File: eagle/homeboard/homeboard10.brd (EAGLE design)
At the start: 100 x 80 mm, 99 parts, among them IC1 XCF02S, IC2 25LC080SN, IC3 ATMEGA32U2-TQFP, Q5 BC848SMD, Q6 BC848SMD, Q7 BC848SMD, Q8 BC848SMD, T1 BSS138, T2 BC848, T3 BSS138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

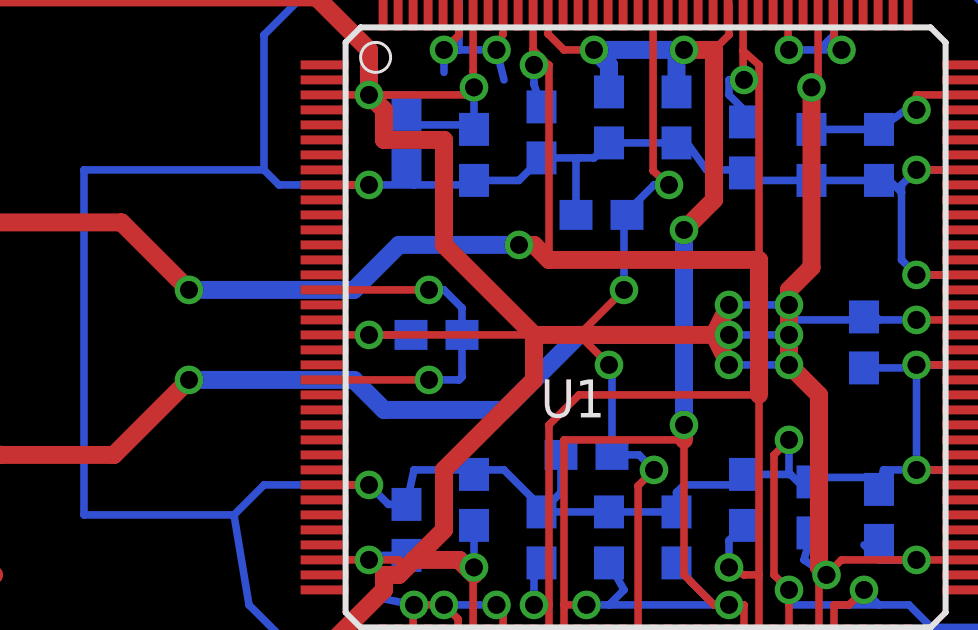
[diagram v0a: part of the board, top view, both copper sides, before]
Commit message: fpga all capactored up
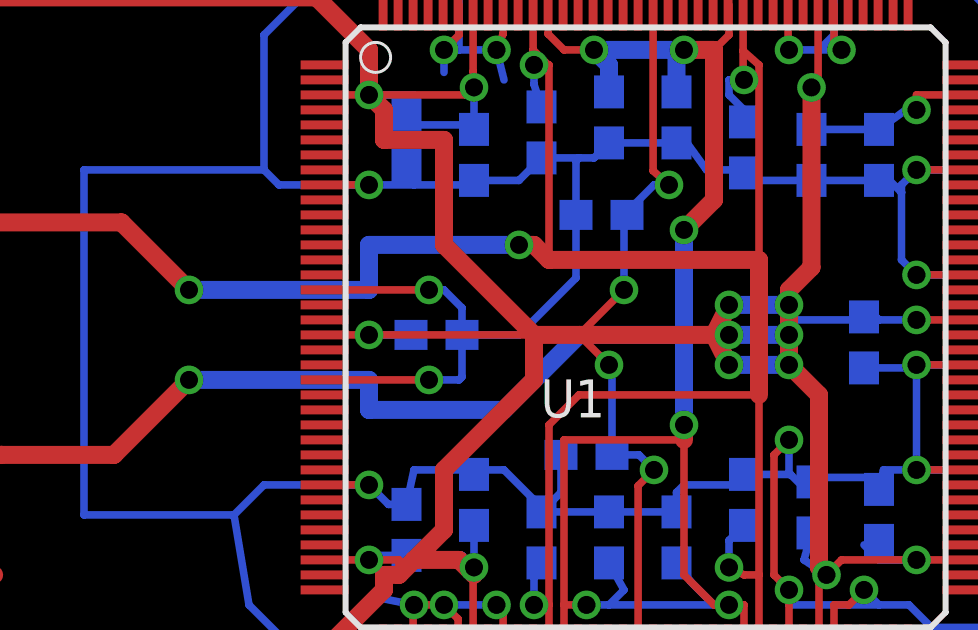
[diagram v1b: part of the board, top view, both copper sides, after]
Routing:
- net GND: track 510.0 -> 516.7 mm
- net VCC: track 334.7 -> 336.7 mm
- net VCCAUX: track 90.3 -> 91.2 mm
- net VCCINT: track 87.4 -> 88.0 mm
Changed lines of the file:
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@@
 <wire x1="29.5" y1="39.5" x2="28.5" y2="39.5" width="0.254" layer="16"/>
 <wire x1="29.6" y1="41" x2="29.6" y2="41.9" width="0.254" layer="16"/>
+<wire x1="33.4" y1="45" x2="33.4" y2="42.9" width="0.254" layer="16"/>
+<wire x1="33.4" y1="42.9" x2="31.5" y2="41" width="0.254" layer="16"/>
+<wire x1="31.5" y1="41" x2="29.6" y2="41" width="0.254" layer="16"/>
 <wire x1="96.05" y1="71" x2="95.55" y2="76" width="0" layer="19" extent="1-1"/>
 <wire x1="96.55" y1="67.5" x2="96.05" y2="71" width="0" layer="19" extent="1-1"/>
@@
 <wire x1="29.47" y1="51.95" x2="29.5" y2="52" width="0" layer="19" extent="1-1"/>
 <wire x1="44.335" y1="7.75" x2="44.5" y2="7.75" width="0" layer="19" extent="1-1"/>
-<wire x1="28.5" y1="39.5" x2="28" y2="36.5" width="0" layer="19" extent="16-16"/>
 <wire x1="98.3" y1="2.25" x2="81.27" y2="16.1284" width="0" layer="19" extent="1-1"/>
 </signal>
@@
 <wire x1="43" y1="41.6" x2="43.4" y2="41.6" width="0.254" layer="16"/>
 <wire x1="43.4" y1="41.6" x2="43.5" y2="41.5" width="0.254" layer="16"/>
-<wire x1="38.5" y1="42" x2="40.5" y2="42" width="0.254" layer="16"/>
-<wire x1="41.5" y1="40" x2="41.5" y2="39" width="0" layer="19" extent="1-16"/>
-<wire x1="41.5" y1="39" x2="40.5" y2="39" width="0" layer="19" extent="1-16"/>
-<wire x1="40.5" y1="42" x2="41.5" y2="40" width="0" layer="19" extent="1-16"/>
-<wire x1="40.5" y1="40" x2="38.5" y2="40" width="0.254" layer="16"/>
-<wire x1="38.5" y1="41" x2="40.5" y2="41" width="0.254" layer="16"/>
+<wire x1="38.5" y1="41" x2="40.5" y2="41" width="0.6" layer="16"/>
 <via x="38.5" y="42" extent="1-16" drill="0.6" shape="square"/>
 <wire x1="38.5" y1="42" x2="38" y2="41" width="0.6" layer="1"/>
@@
 <wire x1="41.5" y1="39" x2="41.5" y2="33.25" width="0.6" layer="1"/>
 <wire x1="41.5" y1="33.25" x2="41.75" y2="33" width="0.6" layer="1"/>
+<wire x1="40.5" y1="40" x2="40.5" y2="41" width="0.6" layer="1"/>
+<via x="40.5" y="41" extent="1-16" drill="0.6" shape="square"/>
+<wire x1="40.5" y1="41" x2="40.5" y2="42" width="0.6" layer="1"/>
+<wire x1="38.5" y1="40" x2="40.5" y2="40" width="0.6" layer="16"/>
+<wire x1="38.5" y1="42" x2="40.5" y2="42" width="0.6" layer="16"/>
+<wire x1="40.5" y1="42" x2="40.5" y2="40" width="0.6" layer="16"/>
 <wire x1="90.9" y1="64.5" x2="92.45" y2="68" width="0" layer="19" extent="1-16"/>
 <wire x1="73.984" y1="67.5094" x2="90.9" y2="64.5" width="0" layer="19" extent="1-16"/>
@@
 <wire x1="35.1" y1="45" x2="35" y2="45" width="0" layer="19" extent="16-16"/>
 <wire x1="18.5" y1="22" x2="18.75" y2="21.85" width="0" layer="19" extent="16-16"/>
-<wire x1="40.5" y1="40" x2="40.5" y2="41" width="0.6" layer="1"/>
-<via x="40.5" y="41" extent="1-16" drill="0.6" shape="square"/>
-<wire x1="40.5" y1="41" x2="40.5" y2="42" width="0.6" layer="1"/>
 </signal>
 <signal name="TCK">
@@
 <wire x1="18" y1="37" x2="20.5" y2="39.5" width="0.6" layer="1"/>
 <via x="20.5" y="39.5" extent="1-16" drill="0.6" shape="square"/>
-<wire x1="20.5" y1="39.5" x2="26" y2="39.5" width="0.6" layer="16"/>
-<wire x1="26" y1="39.5" x2="27" y2="38.5" width="0.6" layer="16"/>
-<wire x1="27" y1="38.5" x2="31" y2="38.5" width="0.6" layer="16"/>
+<wire x1="20.5" y1="39.5" x2="26.5" y2="39.5" width="0.6" layer="16"/>
+<wire x1="26.5" y1="39.5" x2="26.5" y2="38.5" width="0.6" layer="16"/>
+<wire x1="26.5" y1="38.5" x2="31" y2="38.5" width="0.6" layer="16"/>
 <wire x1="31" y1="38.5" x2="33.5" y2="41" width="0.6" layer="16"/>
 <wire x1="33.5" y1="41" x2="37" y2="41" width="0.6" layer="16"/>
@@
 <wire x1="18.25" y1="44.75" x2="20.5" y2="42.5" width="0.6" layer="1"/>
 <via x="20.5" y="42.5" extent="1-16" drill="0.6" shape="square"/>
-<wire x1="20.5" y1="42.5" x2="26" y2="42.5" width="0.6" layer="16"/>
-<wire x1="26" y1="42.5" x2="27.5" y2="44" width="0.6" layer="16"/>
-<wire x1="27.5" y1="44" x2="31.5" y2="44" width="0.6" layer="16"/>
+<wire x1="20.5" y1="42.5" x2="26.5" y2="42.5" width="0.6" layer="16"/>
+<wire x1="26.5" y1="42.5" x2="26.5" y2="44" width="0.6" layer="16"/>
+<wire x1="26.5" y1="44" x2="31.5" y2="44" width="0.6" layer="16"/>
 <via x="31.5" y="44" extent="1-16" drill="0.6" shape="square"/>
 <wire x1="31.5" y1="44" x2="32" y2="44" width="0.6" layer="1"/>

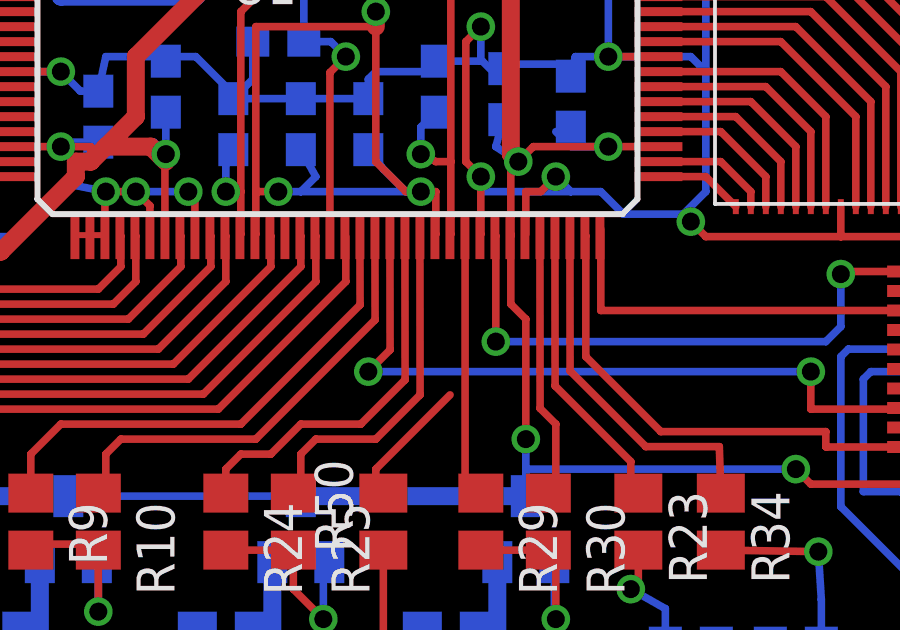
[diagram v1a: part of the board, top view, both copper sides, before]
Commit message: reconnecting blanking pin
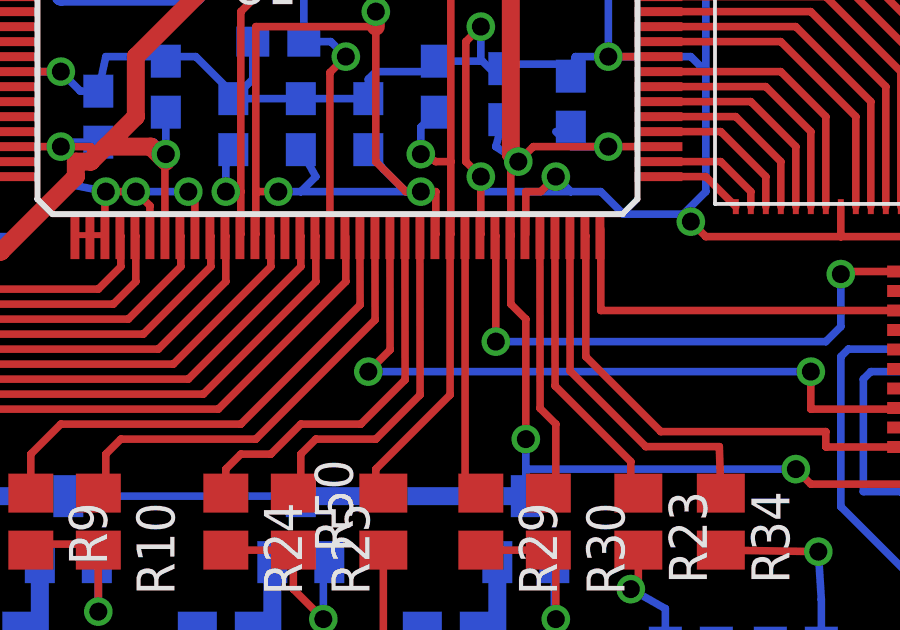
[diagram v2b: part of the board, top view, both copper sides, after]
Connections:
- removed net VCCAUX_R: R50.2
- net VCCAUX: now also R50.2
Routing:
- net VCCAUX: track 91.2 -> 101.4 mm
- net VCCAUX_R: track 4.90 -> 0.00 mm
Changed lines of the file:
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@@
 <wire x1="31.5" y1="44" x2="32" y2="44" width="0.6" layer="1"/>
 <wire x1="32" y1="44" x2="32.5" y2="43.5" width="0.6" layer="1"/>
+<contactref element="R50" pad="2"/>
+<wire x1="39.475" y1="25.225" x2="37" y2="22.75" width="0.254" layer="1"/>
+<wire x1="37" y1="22.75" x2="37" y2="22.25" width="0.254" layer="1"/>
+<wire x1="37" y1="21.75" x2="37" y2="22.25" width="0.254" layer="1"/>
+<wire x1="37.25" y1="21.95" x2="37.25" y2="22" width="0.254" layer="1"/>
+<wire x1="37.25" y1="22" x2="37" y2="22.25" width="0.254" layer="1"/>
 <wire x1="39" y1="48.5" x2="39" y2="48.1" width="0" layer="19" extent="16-16"/>
 <wire x1="11.5" y1="45" x2="11.599" y2="44.75" width="0" layer="19" extent="1-1"/>
+<wire x1="39.475" y1="25.225" x2="39.475" y2="30.545" width="0.254" layer="1"/>
+<wire x1="39.475" y1="30.545" x2="39.47" y2="30.55" width="0.254" layer="1"/>
 </signal>
 <signal name="D_FASTBLANKING">
@@
 <wire x1="5" y1="18" x2="5" y2="18.02" width="0" layer="19" extent="1-1"/>
 </signal>
-<signal name="VCCAUX_R">
-<contactref element="R50" pad="2"/>
-<wire x1="39.475" y1="25.225" x2="37" y2="22.75" width="0.254" layer="1"/>
-<wire x1="37" y1="22.75" x2="37" y2="22.25" width="0.254" layer="1"/>
-<wire x1="37" y1="21.75" x2="37" y2="22.25" width="0.254" layer="1"/>
-<wire x1="37.25" y1="21.95" x2="37.25" y2="22" width="0.254" layer="1"/>
-<wire x1="37.25" y1="22" x2="37" y2="22.25" width="0.254" layer="1"/>
-</signal>
 <signal name="N$67">

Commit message: rework
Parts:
- added R47, R51: 270, rcl:R0805
- moved X3 55.6 mm to (29.5, 74.5), turned to 0 degrees
- moved R5 55.2 mm to (22.0, 64.0), turned to 0 degrees
- moved T1 50.0 mm to (26.0, 63.5), turned to 180 degrees
- moved R4 47.8 mm to (26.0, 60.5), turned to 180 degrees
- moved T3 43.3 mm to (32.0, 63.5), turned to 180 degrees
- moved R6 40.8 mm to (32.0, 60.5), turned to 180 degrees
- moved R7 39.5 mm to (36.0, 64.0), turned to 180 degrees
- moved R1 32.5 mm to (58.3, 55.7)
- moved REG1.2 1.00 mm to (8.50, 36.0)
- moved REG2.5 1.00 mm to (8.50, 43.8)
- moved U$3 1.00 mm to (8.50, 50.8)
- moved U$4 1.00 mm to (8.50, 56.8)
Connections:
- net CLK_5V: now also R47.1
- net DATA_5V: now also R51.1
- net PS2CLK: now also R47.2
- net PS2DAT: now also R51.2
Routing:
- net VCC5: track 69.6 -> 90.8 mm
- net VCC: track 336.7 -> 348.6 mm
- net CLK_5V: track 6.52 -> 9.74 mm
- net PS2CLK: track 1.99 -> 4.58 mm
- net VCCINT: track 88.0 -> 90.5 mm
- net DATA_5V: track 11.0 -> 13.3 mm
- net VCCAUX: track 101.4 -> 103.8 mm
- net PS2DAT: track 1.99 -> 3.78 mm
- net GND: track 516.7 -> 517.8 mm

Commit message: rework
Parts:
- added C26, C27, C28, C29, C30, C31, C32: 100nF, rcl:C0603
- added R53, R54: 22, rcl:R0805
- added X6: MINI-USB_4P-85-32004-10X, con-cypressindustries:85-32004-10X
- moved X1 35.4 mm to (69.5, 15.5), turned to 0 degrees
- moved X5 30.6 mm to (88.0, 64.0)
- moved C2 20.8 mm to (72.0, 70.0)
- moved R11 20.8 mm to (74.9, 58.2)
- moved R12 20.8 mm to (76.5, 60.5)
- moved R17 20.8 mm to (76.0, 72.5)
- moved R18 20.8 mm to (71.0, 74.5)
- moved R19 20.8 mm to (76.5, 67.5)
- moved R21 20.8 mm to (77.0, 64.0)
- moved R22 20.8 mm to (71.0, 64.5)
- moved T2 20.8 mm to (71.5, 61.0)
- moved IC3 5.59 mm to (60.5, 65.0)
- moved IC2 0.50 mm to (5.40, 27.4)
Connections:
- new net N$36: R53.1, X6.2
- new net N$49: IC3.29, R54.2
- new net N$66: R54.1, X6.3
- new net N$68: IC3.30, R53.2
- new net N$69: IC3.28, X6.4
- net GND: now also C26.2, C27.2, C28.2, C29.2, C30.2, C31.2, C32.2, IC3.3
- net VCC: now also C26.1, C27.1, C28.1, C29.1, C30.1, C31.1, C32.1, IC3.31, IC3.32, IC3.4
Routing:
- net GND: track 517.8 -> 541.9 mm, vias 32 -> 34
- net VCC: track 348.6 -> 350.5 mm
- net FL_WP: track 31.6 -> 31.1 mm
- net FL_SEL: track 32.7 -> 32.2 mm
- net FL_SCLK: track 26.8 -> 26.3 mm
- net FL_HOLD: track 30.0 -> 29.5 mm
- net FL_DO: track 31.7 -> 31.2 mm
- net FL_DI: track 24.2 -> 23.7 mm

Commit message: rework
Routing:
- net VCC: track 350.5 -> 354.8 mm
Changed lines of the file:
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@@
 <wire x1="41.5" y1="28.25" x2="41.5" y2="30.525" width="0.254" layer="1"/>
 <wire x1="41.5" y1="30.525" x2="41.47" y2="30.55" width="0.254" layer="1"/>
-<wire x1="25.02" y1="33.5" x2="26.5" y2="33.5" width="0.254" layer="1"/>
-<via x="26.5" y="33.5" extent="1-16" drill="0.6" shape="square"/>
-<wire x1="29.97" y1="30.55" x2="29.97" y2="32.97" width="0.254" layer="1"/>
-<wire x1="29.97" y1="32.97" x2="30" y2="33.25" width="0.254" layer="1"/>
-<via x="30" y="33.25" extent="1-16" drill="0.6" shape="square"/>
-<wire x1="26.65" y1="33.65" x2="26.5" y2="33.5" width="0.254" layer="16"/>
+<via x="26.5" y="34" extent="1-16" drill="0.6" shape="square"/>
 <wire x1="25.02" y1="41" x2="26.5" y2="41" width="0.254" layer="1"/>
 <via x="26.5" y="41" extent="1-16" drill="0.6" shape="square"/>
@@
 <wire x1="41.75" y1="33" x2="42.25" y2="33.5" width="0.254" layer="1"/>
 <wire x1="42.25" y1="33.5" x2="44.75" y2="33.5" width="0.254" layer="1"/>
-<wire x1="30" y1="33.25" x2="30" y2="33" width="0.254" layer="16"/>
-<wire x1="30" y1="33.25" x2="29.6" y2="33.65" width="0.254" layer="16"/>
 <via x="36" y="36.5" extent="1-16" drill="0.6" shape="square"/>
 <wire x1="35.5" y1="37" x2="36" y2="36.5" width="0.254" layer="16"/>
 <wire x1="30" y1="49.25" x2="30" y2="48" width="0.254" layer="16"/>
 <wire x1="30" y1="48" x2="28.1" y2="48" width="0.254" layer="16"/>
-<wire x1="41.47" y1="51.95" x2="41.47" y2="49.47" width="0.254" layer="1"/>
-<via x="41.25" y="49.25" extent="1-16" drill="0.6" shape="square"/>
+<via x="40.75" y="49.25" extent="1-16" drill="0.6" shape="square"/>
 <wire x1="41.25" y1="48.25" x2="41.5" y2="48" width="0.254" layer="16"/>
-<wire x1="41.47" y1="49.47" x2="41.25" y2="49.25" width="0.254" layer="1"/>
-<wire x1="41.25" y1="48.25" x2="41.25" y2="49.25" width="0.254" layer="16"/>
-<wire x1="41.35" y1="47.85" x2="41.5" y2="48" width="0.254" layer="16"/>
+<wire x1="41.25" y1="48.25" x2="40.75" y2="49.25" width="0.254" layer="16"/>
 <wire x1="35.97" y1="51.95" x2="35.97" y2="46.47" width="0.254" layer="1"/>
 <wire x1="35.97" y1="46.47" x2="36.5" y2="46" width="0.254" layer="1"/>
@@
 <wire x1="32" y1="41" x2="32" y2="39.5" width="0.6" layer="1"/>
 <wire x1="32" y1="39.5" x2="29" y2="36.5" width="0.6" layer="1"/>
-<wire x1="29" y1="36.5" x2="29" y2="34.5" width="0.6" layer="1"/>
-<wire x1="29" y1="34.5" x2="28" y2="33.5" width="0.6" layer="1"/>
-<wire x1="27.5" y1="33" x2="27.5" y2="33.5" width="0.254" layer="1"/>
-<wire x1="27.5" y1="33.5" x2="26.5" y2="33.5" width="0.254" layer="1"/>
-<wire x1="27.5" y1="33" x2="27" y2="33" width="0.6" layer="1"/>
-<wire x1="27" y1="33" x2="27" y2="32.5" width="0.6" layer="1"/>
-<wire x1="27" y1="32.5" x2="24.5" y2="30" width="0.6" layer="1"/>
-<wire x1="24.5" y1="30" x2="23.5" y2="30" width="0.6" layer="1"/>
-<wire x1="27.5" y1="33" x2="28" y2="33.5" width="0.6" layer="1"/>
-<wire x1="28" y1="33.5" x2="29.5" y2="33.5" width="0.6" layer="1"/>
-<wire x1="29.5" y1="33.5" x2="30" y2="33" width="0.6" layer="1"/>
 <wire x1="35.47" y1="30.55" x2="35.47" y2="35.97" width="0.254" layer="1"/>
 <wire x1="35.47" y1="35.97" x2="36" y2="36.5" width="0.254" layer="1"/>
@@
 <wire x1="40.5" y1="42.5" x2="41.25" y2="43.25" width="0.6" layer="1"/>
 <wire x1="41.25" y1="43.25" x2="41.25" y2="49.25" width="0.6" layer="1"/>
+<wire x1="41.25" y1="49.25" x2="40.75" y2="49.25" width="0.6" layer="1"/>
 <via x="40.5" y="40" extent="1-16" drill="0.6" shape="square"/>
 <wire x1="40.5" y1="40" x2="41.5" y2="39" width="0.6" layer="1"/>
@@
 <contactref element="IC3" pad="31"/>
 <contactref element="IC3" pad="4"/>
+<wire x1="29.97" y1="30.55" x2="29.97" y2="33" width="0.254" layer="1"/>
+<wire x1="29.97" y1="33" x2="29.97" y2="33.22" width="0.254" layer="1"/>
+<wire x1="29.97" y1="33.22" x2="30.25" y2="33.25" width="0.254" layer="1"/>
+<via x="30.25" y="33.25" extent="1-16" drill="0.6" shape="square"/>
+<wire x1="30.25" y1="33.25" x2="30" y2="34.65" width="0.254" layer="16"/>
+<wire x1="25.02" y1="33.5" x2="26.5" y2="33.5" width="0.254" layer="1"/>
+<wire x1="26.5" y1="33.5" x2="26.5" y2="34" width="0.254" layer="1"/>
+<wire x1="27" y1="33.5" x2="26.5" y2="34" width="0.254" layer="16"/>
+<wire x1="30" y1="34.65" x2="30" y2="34.5" width="0.254" layer="16"/>
+<wire x1="30" y1="34.5" x2="29" y2="33.5" width="0.254" layer="16"/>
+<wire x1="29" y1="33.5" x2="27.9" y2="33.5" width="0.254" layer="16"/>
+<wire x1="27.9" y1="33.5" x2="27.75" y2="33.65" width="0.254" layer="16"/>
+<wire x1="27" y1="33.5" x2="27.6" y2="33.5" width="0.254" layer="16"/>
+<wire x1="27.6" y1="33.5" x2="27.75" y2="33.65" width="0.254" layer="16"/>
+<wire x1="29" y1="36.5" x2="29" y2="33" width="0.6" layer="1"/>
+<wire x1="29" y1="33" x2="27" y2="33" width="0.6" layer="1"/>
+<wire x1="27" y1="33" x2="27" y2="32.5" width="0.6" layer="1"/>
+<wire x1="27" y1="32.5" x2="24.5" y2="30" width="0.6" layer="1"/>
+<wire x1="29" y1="33" x2="29.97" y2="33" width="0.6" layer="1"/>
+<wire x1="41.25" y1="47.85" x2="41.35" y2="47.85" width="0.254" layer="16"/>
+<wire x1="41.35" y1="47.85" x2="41.5" y2="48" width="0.254" layer="16"/>
+<wire x1="41.5" y1="49" x2="40.75" y2="49.25" width="0.254" layer="1"/>
+<wire x1="41.47" y1="51.95" x2="41.47" y2="49.03" width="0.254" layer="1"/>
+<wire x1="41.47" y1="49.03" x2="41.5" y2="49" width="0.254" layer="1"/>
 <wire x1="70.4" y1="61" x2="71.95" y2="64.5" width="0" layer="19" extent="1-16"/>
 <wire x1="71.65" y1="49" x2="70.4" y2="61" width="0" layer="19" extent="1-1"/>
@@
 <wire x1="72.15" y1="35" x2="71.65" y2="39" width="0" layer="19" extent="1-1"/>
 <wire x1="61.5" y1="51.35" x2="71.65" y2="49" width="0" layer="19" extent="1-1"/>
-<wire x1="41.25" y1="49.25" x2="41.5" y2="49" width="0" layer="19" extent="1-16"/>
-<wire x1="30" y1="33" x2="30" y2="33" width="0" layer="19" extent="1-16"/>
-<wire x1="41.25" y1="47.85" x2="41.35" y2="47.85" width="0" layer="19" extent="16-16"/>
 <wire x1="35.1" y1="45" x2="35" y2="45" width="0" layer="19" extent="16-16"/>
 <wire x1="30" y1="47.85" x2="30" y2="48" width="0" layer="19" extent="16-16"/>
 <wire x1="61.5" y1="29.5" x2="61.393396875" y2="29.337409375" width="0" layer="19" extent="1-1"/>
-<wire x1="27.75" y1="33.65" x2="27.5" y2="33.5" width="0" layer="19" extent="1-16"/>
 <wire x1="18.5" y1="22" x2="18.75" y2="21.85" width="0" layer="19" extent="16-16"/>
 <wire x1="43" y1="41.6" x2="43.4" y2="41.6" width="0" layer="19" extent="16-16"/>
@@
 <wire x1="11.1" y1="50.115" x2="11.735" y2="50.75" width="0" layer="19" extent="1-1"/>
 <wire x1="41.25" y1="34.4" x2="41" y2="33.5" width="0" layer="19" extent="16-16"/>
-<wire x1="30" y1="34.65" x2="29" y2="34.5" width="0" layer="19" extent="1-16"/>
 <wire x1="27.9" y1="41" x2="26.5" y2="41" width="0" layer="19" extent="1-16"/>
 <wire x1="11.599" y1="56.75" x2="13.5" y2="56.75" width="0" layer="19" extent="1-1"/>
@@
 <wire x1="38.97" y1="49.53" x2="39" y2="49.5" width="0.254" layer="1"/>
 <via x="39" y="49.5" extent="1-16" drill="0.6" shape="square"/>
-<wire x1="39" y1="49.5" x2="38.5" y2="49.5" width="0.254" layer="16"/>
-<wire x1="38.5" y1="49.5" x2="38.5" y2="49" width="0.254" layer="16"/>
-<wire x1="38.5" y1="49" x2="39" y2="48.5" width="0.254" layer="16"/>
 <wire x1="32.5" y1="50" x2="32.5" y2="43.5" width="0.254" layer="1"/>
 <wire x1="39.5" y1="50" x2="39.5" y2="43.5" width="0.254" layer="1"/>
@@
 <wire x1="39.475" y1="25.225" x2="39.475" y2="30.545" width="0.254" layer="1"/>
 <wire x1="39.475" y1="30.545" x2="39.47" y2="30.55" width="0.254" layer="1"/>
-<wire x1="39" y1="48.5" x2="39" y2="48.1" width="0" layer="19" extent="16-16"/>
+<wire x1="39" y1="48.1" x2="39" y2="48" width="0.254" layer="16"/>
+<wire x1="39" y1="48.1" x2="39" y2="49.5" width="0.254" layer="16"/>
 <wire x1="11.5" y1="44" x2="11.599" y2="43.75" width="0" layer="19" extent="1-1"/>
 </signal>

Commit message: power socket
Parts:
- added X8: DC21MMX, powersupply:DC-21MM
- moved X1 64.7 mm to (49.5, 77.0)
- moved X6 9.50 mm to (38.0, 69.8)
- moved R4 7.54 mm to (18.5, 61.2)
- moved R47 7.54 mm to (15.2, 61.5)
- moved R5 7.54 mm to (14.5, 64.8)
- moved R51 7.54 mm to (22.0, 64.8)
- moved R6 7.54 mm to (24.5, 61.2)
- moved R7 7.54 mm to (28.5, 64.8)
- moved T1 7.54 mm to (18.5, 64.2)
- moved T3 7.54 mm to (24.5, 64.2)
- moved X3 7.54 mm to (22.0, 75.2)
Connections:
- net GND: now also X8.1, X8.3
- net VCC5: now also X8.2
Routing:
- net GND: track 541.9 -> 565.0 mm
- net VCC: track 354.8 -> 369.0 mm
- net VCC5: track 90.8 -> 88.7 mm
- net PS2DAT: track 3.78 -> 4.76 mm
